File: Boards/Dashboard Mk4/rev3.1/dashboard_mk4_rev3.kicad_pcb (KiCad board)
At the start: 2 copper layers, 87.9 x 50.6 mm, 58 parts, among them J1 MM_F_VT_10, J2 MM_F_VT_20, J3 MM_F_VT_04, J4 CONN_02X03, J5 CONN_02X03, U1 ATMEGA16M1, U2 TPS561201, U3 ATmega328P-AU, U4 CAN_Transceiver, Y1 Crystal_SMD, Y2 Crystal_SMD

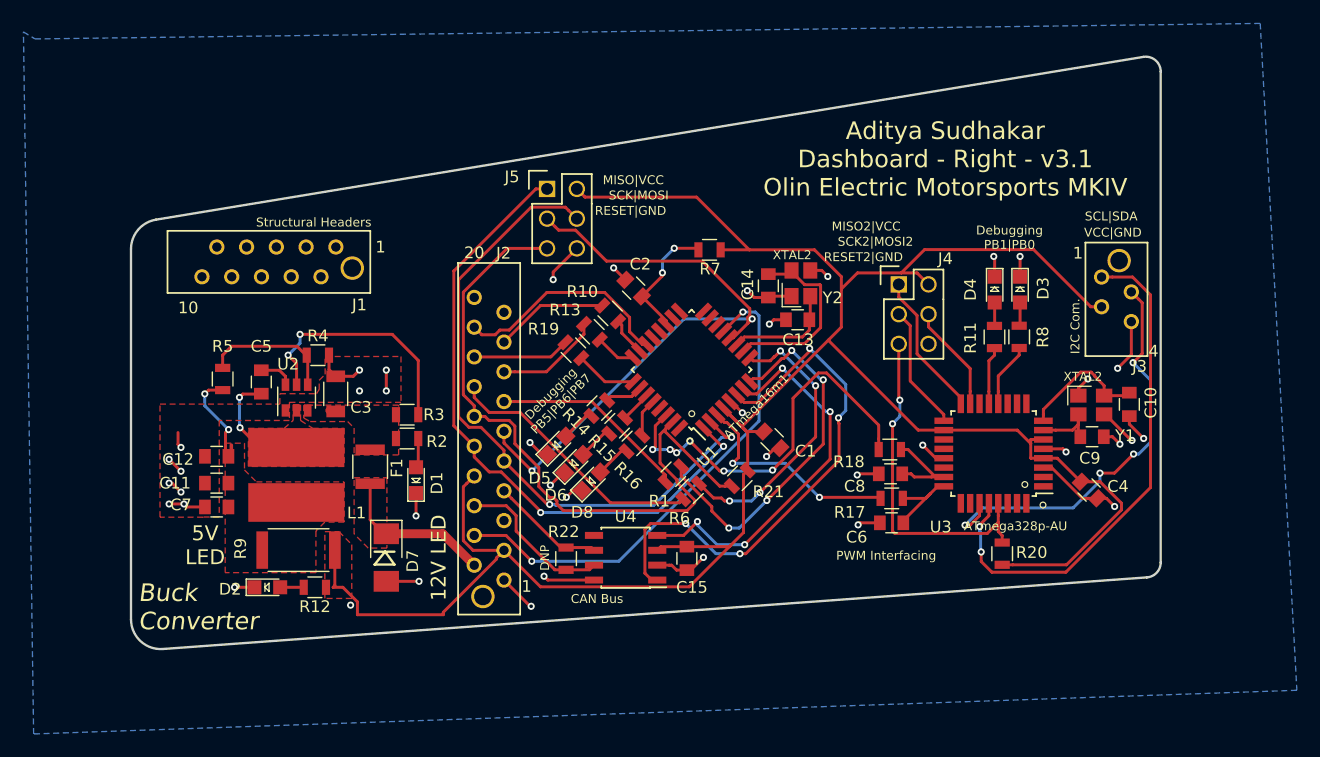
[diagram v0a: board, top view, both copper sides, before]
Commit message: Dashboard Layout v3.1 and v4.0
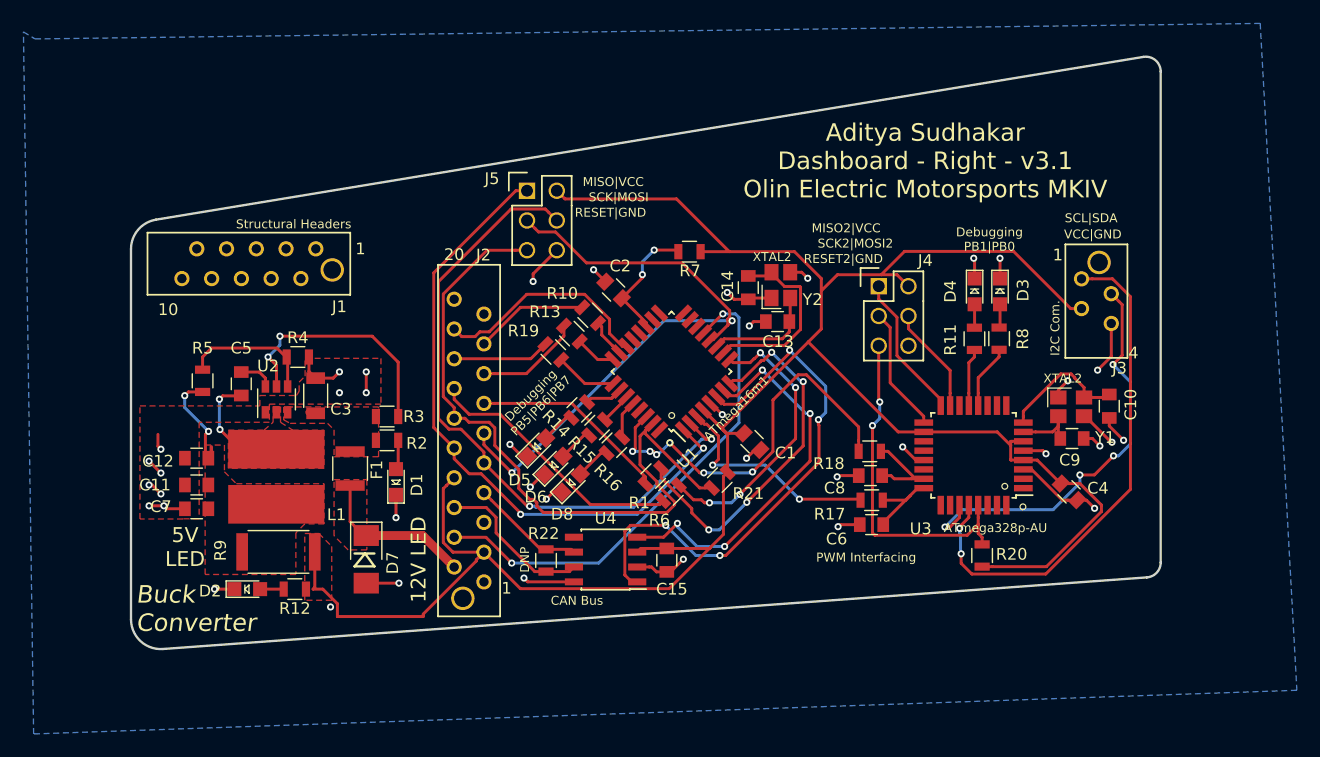
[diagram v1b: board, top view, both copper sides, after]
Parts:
- moved C13 1.72 mm to (83.4, 46.2)
- moved C6 1.72 mm to (91.5, 63.5)
- moved C8 1.72 mm to (91.4, 59.3)
- moved D3 1.72 mm to (102.4, 43.6)
- moved D5 1.72 mm to (62.9, 56.9)
- moved R18 1.72 mm to (91.3, 57.2)
- moved R5 1.72 mm to (34.4, 51.2)
- moved R6 1.72 mm to (74.3, 60.8)
- moved R8 1.72 mm to (102.3, 47.6)
- moved U3 1.72 mm to (100.2, 57.6)
- moved C1 1.72 mm to (81.3, 56.4)
- moved C15 1.72 mm to (74.0, 66.5)
- moved C3 1.72 mm to (44.0, 52.5)
- moved C4 1.72 mm to (108.3, 60.7)
- moved D2 1.72 mm to (38.2, 69.0)
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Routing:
- net GND: track 85.3 -> 82.0 mm, vias 40 -> 39
